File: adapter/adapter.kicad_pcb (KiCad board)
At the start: 2 copper layers, 43.5 x 38.6 mm, 20 parts, among them J1 Conn_01x06_Female, SW1 RotaryEncoder_Switch

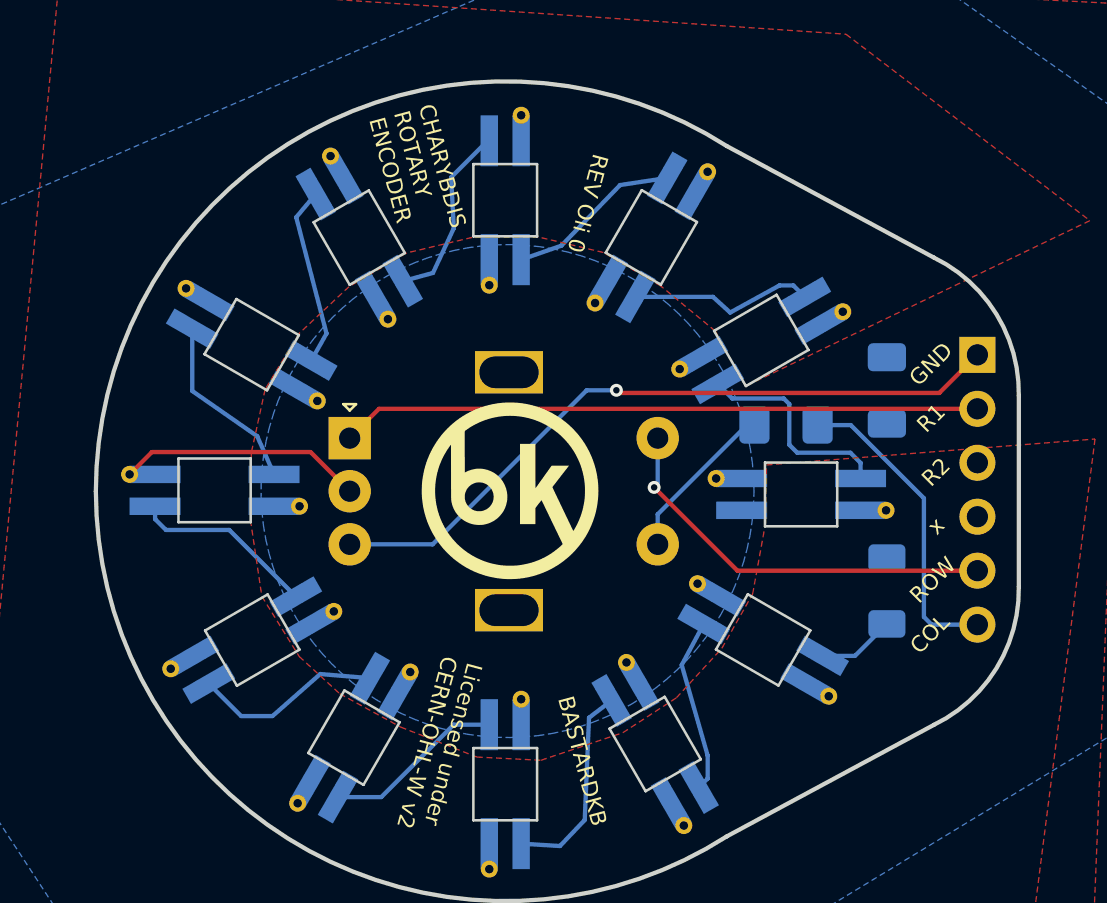
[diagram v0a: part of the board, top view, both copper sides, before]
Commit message: route without break
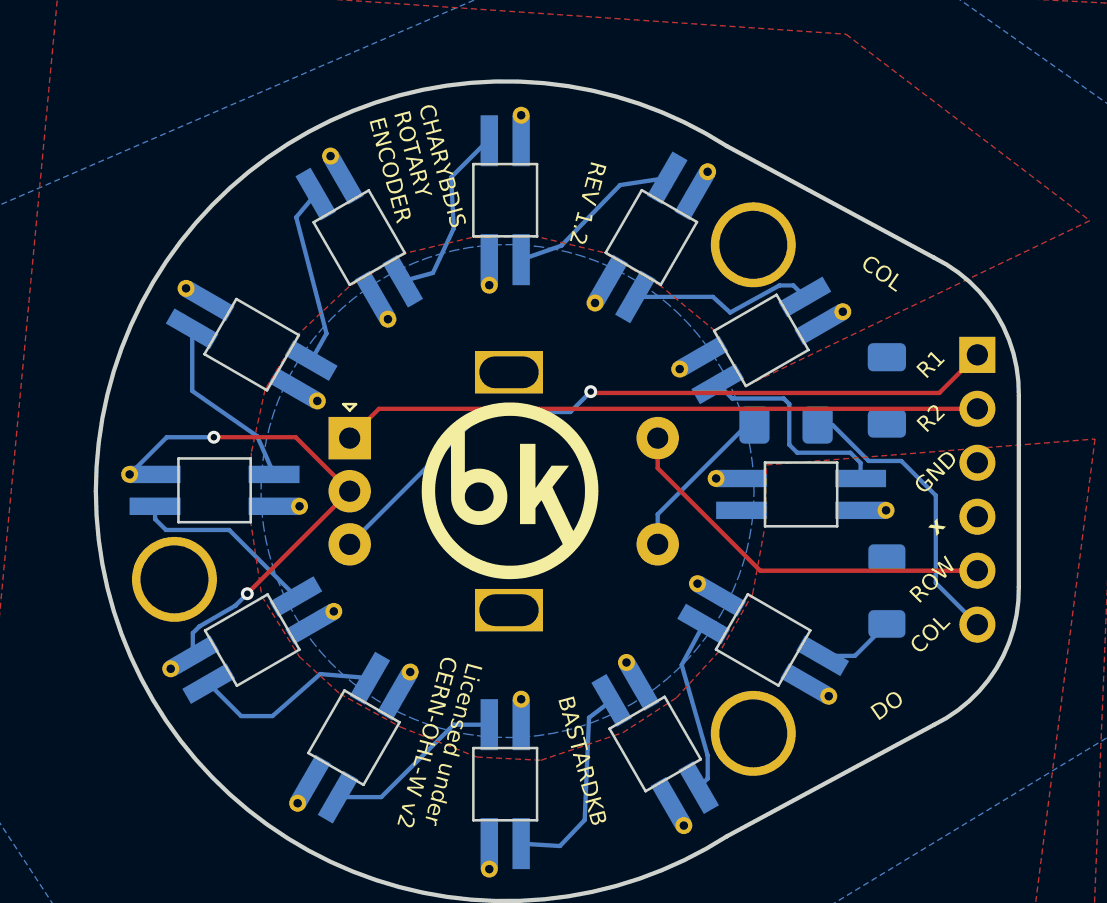
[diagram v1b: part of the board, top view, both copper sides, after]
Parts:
- added ?: , , F.Cu at (64.0, 55.0)
- added ?: , , F.Cu at (36.8, 47.8)
- added ?: , , F.Cu at (64.0, 32.0)
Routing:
- net Gnd: track 11.6 -> 23.2 mm, vias 0 -> 2
- net Col: track 14.7 -> 13.8 mm
- net DIN: track 0.84 -> 0.00 mm
- net button: track 19.2 -> 18.5 mm, vias 1 -> 0
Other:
- board text added: "DO"
- board text added: "REV 1.2"
- board text removed: "REV Oli 0"
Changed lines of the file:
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@@
       (drillshape 0)
       (scaleselection 1)
-      (outputdirectory "gerber")
+      (outputdirectory "../../Charybdis-EC11-rev1-2_gerbers/")
     )
   )
@@
       (net 2 "Gnd") (pinfunction "Pin_3") (pintype "passive"))
     (pad "4" thru_hole oval locked (at 0 1.2) (size 1.7 1.7) (drill 1) (layers "*.Cu" "*.Mask")
-      (net 22 "unconnected-(J1-Pin_4-Pad4)") (pinfunction "Pin_4") (pintype "passive"))
+      (net 22 "unconnected-(J1-Pin_4-Pad4)") (pinfunction "Pin_4") (pintype "passive+no_connect"))
     (pad "5" thru_hole oval locked (at 0 3.74) (size 1.7 1.7) (drill 1) (layers "*.Cu" "*.Mask")
       (net 16 "button") (pinfunction "Pin_5") (pintype "passive"))
@@
     )
   )
+  (footprint "" (layer "F.Cu")
+    (at 64 55)
+    (fp_text reference "" (at 0 0) (layer "F.SilkS")
+        (effects (font (size 1.27 1.27) (thickness 0.15)))
+    )
+    (fp_text value "" (at 0 0) (layer "F.SilkS")
+        (effects (font (size 1.27 1.27) (thickness 0.15)))
+    )
+    (pad "1" thru_hole circle (at 0 0) (size 4 4) (drill 3.2) (layers "*.Cu" "*.Mask"))
+  )
+  (footprint "" (layer "F.Cu")
+    (at 36.75 47.75)
+    (fp_text reference "" (at 0 0) (layer "F.SilkS")
+        (effects (font (size 1.27 1.27) (thickness 0.15)))
+    )
+    (fp_text value "" (at 0 0) (layer "F.SilkS")
+        (effects (font (size 1.27 1.27) (thickness 0.15)))
+    )
+    (pad "1" thru_hole circle (at 0 0) (size 4 4) (drill 3.2) (layers "*.Cu" "*.Mask"))
+  )
+  (footprint "" (layer "F.Cu")
+    (at 64 32)
+    (fp_text reference "" (at 0 0) (layer "F.SilkS")
+        (effects (font (size 1.27 1.27) (thickness 0.15)))
+    )
+    (fp_text value "" (at 0 0) (layer "F.SilkS")
+        (effects (font (size 1.27 1.27) (thickness 0.15)))
+    )
+    (pad "1" thru_hole circle (at 0 0) (size 4 4) (drill 3.2) (layers "*.Cu" "*.Mask"))
+  )
   (footprint "Library:YS-SK6812MINI-E" (layer "B.Cu")
     (at 40.414 50.608 30)
@@
   )
   (gr_text "x" (at 72.583426 45.227764 45) (layer "B.SilkS" knockout)
-    (effects (font (size 0.75 0.75) (thickness 0.1)) (justify mirror))
+    (effects (font (size 0.75 0.75) (thickness 0.15) bold) (justify mirror))
   )
   (gr_text "330" (at 68.77 48.371 90) (layer "B.SilkS")
@@
     (effects (font (size 0.75 0.75) (thickness 0.1)) (justify left))
   )
-  (gr_text "R2" (at 72.6 42.7 45) (layer "F.SilkS")
+  (gr_text "GND" (at 72.6 42.7 45) (layer "F.SilkS")
     (effects (font (size 0.75 0.75) (thickness 0.1)))
   )
@@
     (effects (font (size 0.75 0.75) (thickness 0.1)))
   )
-  (gr_text "R1" (at 72.372715 40.160001 45) (layer "F.SilkS")
+  (gr_text "R2" (at 72.372715 40.160001 45) (layer "F.SilkS")
     (effects (font (size 0.75 0.75) (thickness 0.1)))
   )
@@
     (effects (font (size 0.75 0.75) (thickness 0.1)))
   )
+  (gr_text "COL" (at 70.063328 33.336 -35) (layer "F.SilkS")
+    (effects (font (size 0.75 0.75) (thickness 0.1)))
+  )
+  (gr_text "DO" (at 70.312 53.692 35) (layer "F.SilkS")
+    (effects (font (size 0.75 0.75) (thickness 0.1)))
+  )
   (gr_text "CHARYBDIS \nROTARY \nENCODER" (at 47.413 25.707 285) (layer "F.SilkS")
     (effects (font (size 0.75 0.75) (thickness 0.1)) (justify left))
   )
-  (gr_text "GND" (at 72.360088 37.620001 45) (layer "F.SilkS")
+  (gr_text "R1" (at 72.360088 37.620001 45) (layer "F.SilkS")
     (effects (font (size 0.75 0.75) (thickness 0.1)))
   )
-  (gr_text "x" (at 72.6 45.24 45) (layer "F.SilkS")
-    (effects (font (size 0.75 0.75) (thickness 0.1)))
+  (gr_text "x" (at 72.6 45.24 45) (layer "F.SilkS" knockout)
+    (effects (font (size 0.75 0.75) (thickness 0.15) bold))
   )
   (gr_text "ROW" (at 72.448477 47.78 45) (layer "F.SilkS")
     (effects (font (size 0.75 0.75) (thickness 0.1)))
   )
-  (gr_text "REV Oli 0" (at 56.2 30.05 255) (layer "F.SilkS")
+  (gr_text "REV 1.2" (at 56.2 30.05 255) (layer "F.SilkS")
     (effects (font (size 0.75 0.75) (thickness 0.1)))
   )
-  (segment (start 43.1564 41.7564) (end 35.6906 41.7564) (width 0.2032) (layer "F.Cu") (net 2))
-  (segment (start 45 43.6) (end 43.1564 41.7564) (width 0.2032) (layer "F.Cu") (net 2))
-  (segment (start 35.6906 41.7564) (end 34.639 42.808) (width 0.2032) (layer "F.Cu") (net 2))
+  (segment (start 42.4578 41.0578) (end 38.6056 41.0578) (width 0.2032) (layer "F.Cu") (net 2))
+  (segment (start 45 43.6) (end 40.1804 48.4196) (width 0.2032) (layer "F.Cu") (net 2))
+  (segment (start 45 43.6) (end 42.4578 41.0578) (width 0.2032) (layer "F.Cu") (net 2))
+  (segment (start 40.1804 48.4196) (end 40.1804 48.4238) (width 0.2032) (layer "F.Cu") (net 2))
+  (via (at 40.1804 48.4238) (size 0.6096) (drill 0.3048) (layers "F.Cu" "B.Cu") (net 2))
+  (via (at 38.6056 41.0578) (size 0.6096) (drill 0.3048) (layers "F.Cu" "B.Cu") (net 2))
+  (segment (start 37.932767 49.960233) (end 37.614129 50.278871) (width 0.2032) (layer "B.Cu") (net 2))
+  (segment (start 38.6056 41.0578) (end 36.3892 41.0578) (width 0.2032) (layer "B.Cu") (net 2))
+  (segment (start 40.1804 48.4238) (end 39.615486 48.988714) (width 0.2032) (layer "B.Cu") (net 2))
+  (segment (start 39.615486 48.988714) (end 37.932767 49.960233) (width 0.2032) (layer "B.Cu") (net 2))
+  (segment (start 36.3892 41.0578) (end 34.639 42.808) (width 0.2032) (layer "B.Cu") (net 2))
+  (segment (start 37.614129 50.278871) (end 37.614129 51.358481) (width 0.2032) (layer "B.Cu") (net 2))
   (segment (start 60.629 51.779) (end 61.85218 56.044101) (width 0.2032) (layer "B.Cu") (net 3))
   (segment (start 61.85218 57.12721) (end 61.429519 57.549871) (width 0.2032) (layer "B.Cu") (net 3))
@@
   (segment (start 68.572 41.787) (end 69.05 42.265) (width 0.2032) (layer "B.Cu") (net 15))
   (segment (start 63.01061 39.235) (end 65.434 39.235) (width 0.2032) (layer "B.Cu") (net 15))
-  (segment (start 63.252 47.34) (end 74.55 47.34) (width 0.2032) (layer "F.Cu") (net 16))
-  (segment (start 59.332 43.42) (end 63.252 47.34) (width 0.2032) (layer "F.Cu") (net 16))
-  (via (at 59.332 43.42) (size 0.6096) (drill 0.3048) (layers "F.Cu" "B.Cu") (net 16))
-  (segment (start 59.5 43.252) (end 59.332 43.42) (width 0.2032) (layer "B.Cu") (net 16))
-  (segment (start 59.5 41.1) (end 59.5 43.252) (width 0.2032) (layer "B.Cu") (net 16))
-  (segment (start 57.554 38.848) (end 57.678695 38.972695) (width 0.2032) (layer "F.Cu") (net 17))
-  (segment (start 57.678695 38.972695) (end 72.757305 38.972695) (width 0.2032) (layer "F.Cu") (net 17))
+  (segment (start 59.5 42.514213) (end 64.325787 47.34) (width 0.2032) (layer "F.Cu") (net 16))
+  (segment (start 64.325787 47.34) (end 74.55 47.34) (width 0.2032) (layer "F.Cu") (net 16))
+  (segment (start 59.5 41.1) (end 59.5 42.514213) (width 0.2032) (layer "F.Cu") (net 16))
+  (segment (start 56.3475 38.9115) (end 56.408695 38.972695) (width 0.2032) (layer "F.Cu") (net 17))
+  (segment (start 56.408695 38.972695) (end 72.757305 38.972695) (width 0.2032) (layer "F.Cu") (net 17))
   (segment (start 72.757305 38.972695) (end 74.55 37.18) (width 0.2032) (layer "F.Cu") (net 17))
-  (via (at 57.554 38.848) (size 0.6096) (drill 0.3048) (layers "F.Cu" "B.Cu") (net 17))
-  (segment (start 56.157 38.848) (end 48.905 46.1) (width 0.2032) (layer "B.Cu") (net 17))
-  (segment (start 57.554 38.848) (end 56.157 38.848) (width 0.2032) (layer "B.Cu") (net 17))
-  (segment (start 48.905 46.1) (end 45 46.1) (width 0.2032) (layer "B.Cu") (net 17))
+  (via (at 56.3475 38.9115) (size 0.6096) (drill 0.3048) (layers "F.Cu" "B.Cu") (net 17))
+  (segment (start 56.3475 38.9115) (end 55.3876 39.8714) (width 0.2032) (layer "B.Cu") (net 17))
+  (segment (start 51.2286 39.8714) (end 45 46.1) (width 0.2032) (layer "B.Cu") (net 17))
+  (segment (start 55.3876 39.8714) (end 51.2286 39.8714) (width 0.2032) (layer "B.Cu") (net 17))
   (segment (start 46.38 39.72) (end 74.55 39.72) (width 0.2032) (layer "F.Cu") (net 18))
   (segment (start 45 41.1) (end 46.38 39.72) (width 0.2032) (layer "F.Cu") (net 18))
-  (segment (start 70.882 47.34) (end 70.289 46.747) (width 0.2032) (layer "B.Cu") (net 19))
-  (segment (start 72.032 43.928) (end 72.032 49.516) (width 0.2032) (layer "B.Cu") (net 20))
-  (segment (start 67.027 40.487) (end 68.591 40.487) (width 0.2032) (layer "B.Cu") (net 20))
-  (segment (start 68.591 40.487) (end 72.032 43.928) (width 0.2032) (layer "B.Cu") (net 20))
-  (segment (start 72.032 49.516) (end 72.396 49.88) (width 0.2032) (layer "B.Cu") (net 20))
-  (segment (start 72.396 49.88) (end 74.55 49.88) (width 0.2032) (layer "B.Cu") (net 20))
-  (segment (start 63.698787 40.487) (end 64.052 40.487) (width 0.2032) (layer "B.Cu") (net 21))
+  (segment (start 70.9652 42.1754) (end 72.5908 43.801) (width 0.2032) (layer "B.Cu") (net 20))
+  (segment (start 67.738973 40.487) (end 69.427373 42.1754) (width 0.2032) (layer "B.Cu") (net 20))
+  (segment (start 74.55 49.88) (end 72.5908 47.9208) (width 0.2032) (layer "B.Cu") (net 20))
+  (segment (start 69.427373 42.1754) (end 70.9652 42.1754) (width 0.2032) (layer "B.Cu") (net 20))
+  (segment (start 72.5908 47.9208) (end 72.5908 43.801) (width 0.2032) (layer "B.Cu") (net 20))
+  (segment (start 67.027 40.487) (end 67.738973 40.487) (width 0.2032) (layer "B.Cu") (net 20))
   (segment (start 59.5 46.1) (end 59.5 44.685787) (width 0.2032) (layer "B.Cu") (net 21))
   (segment (start 59.5 44.685787) (end 63.698787 40.487) (width 0.2032) (layer "B.Cu") (net 21))
-  (segment (start 74.139 44.8) (end 74.55 44.8) (width 0.2032) (layer "F.Cu") (net 22))
+  (segment (start 63.698787 40.487) (end 64.052 40.487) (width 0.2032) (layer "B.Cu") (net 21))
   (zone (net 2) (net_name "Gnd") (layer "F.Cu") (hatch edge 0.508)
     (priority 10)
